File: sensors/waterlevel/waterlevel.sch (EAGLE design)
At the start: 77 parts, among them IC2 MCP604SL, IC3 MCP601SN, IC4 MCP601SN, P1 CAMDEN-CTB5000/6, U1 NCP1729SN35T1G, U2 SR05S05, U3 VISHAY-VCUT05A4, U4 VISHAY-VCUT05A4, U5 LP3981IMM-3.3

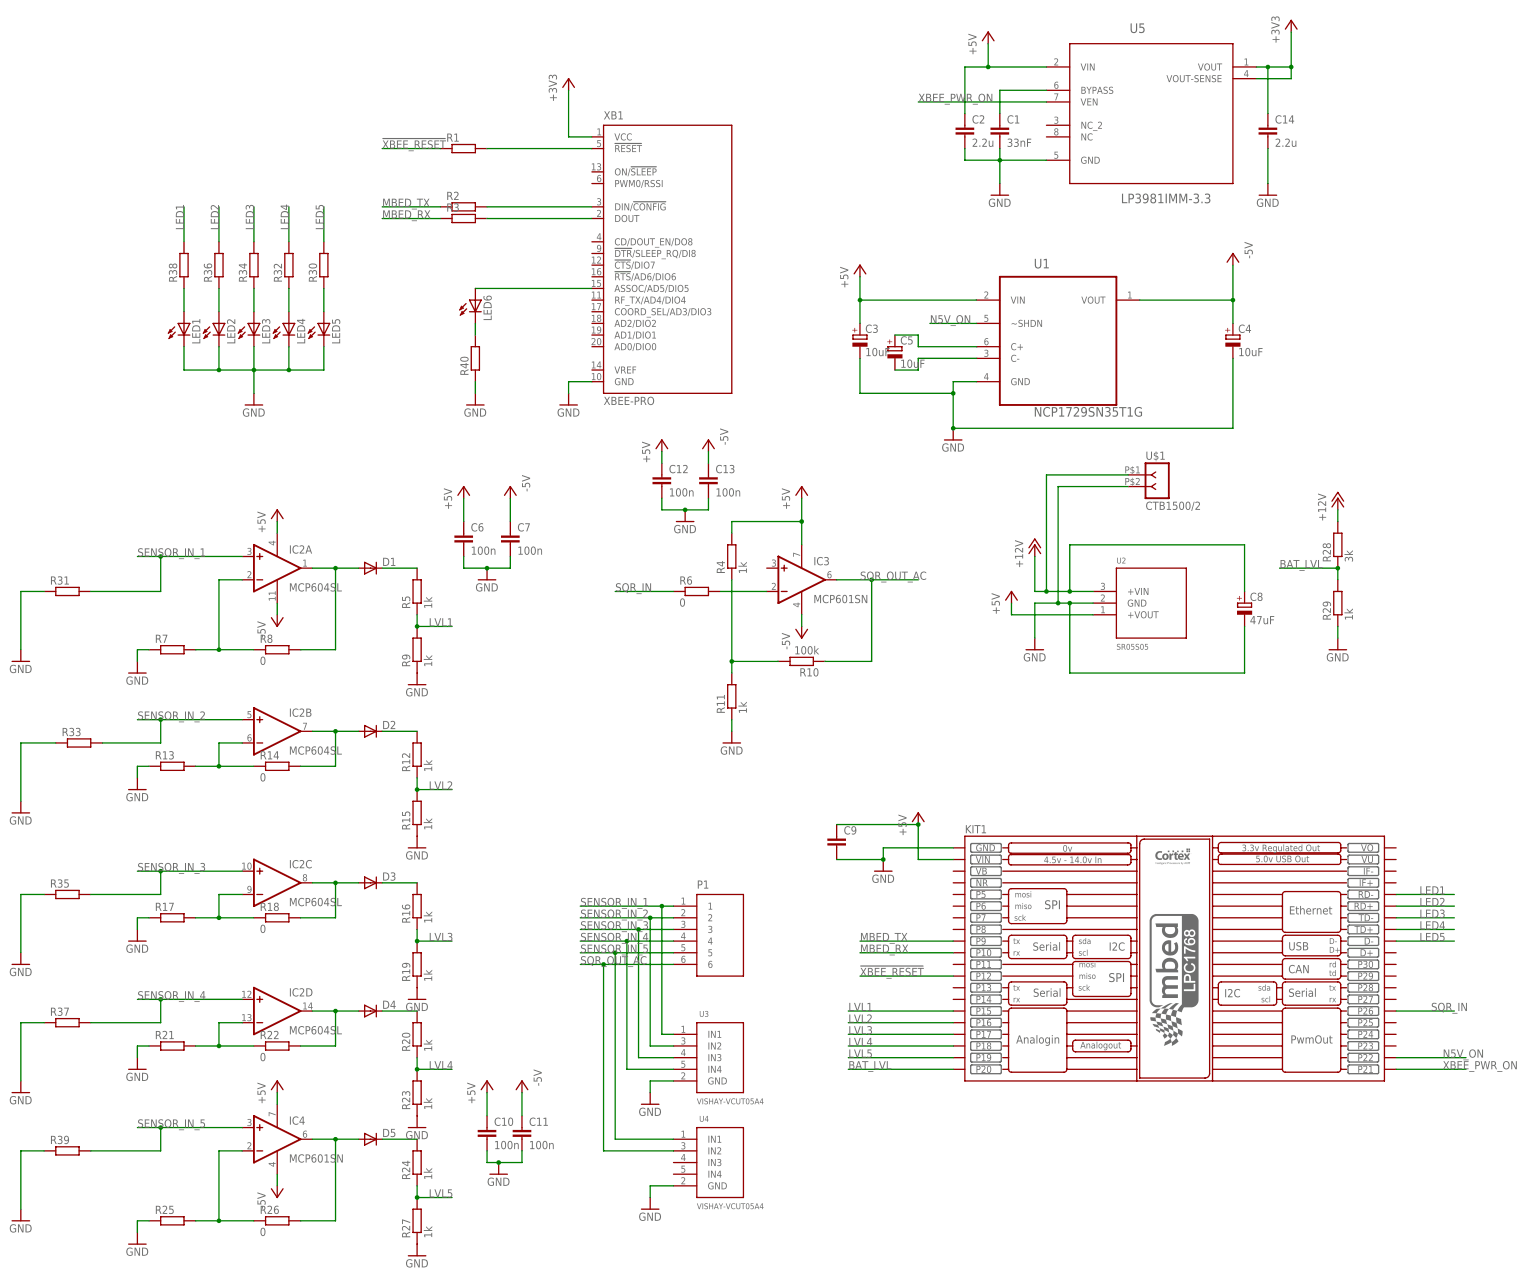
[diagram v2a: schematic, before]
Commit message: Completed water level sensor / wireless network board.
Added status LEDs
Added test points for critical signals
Added M3 mounting holes
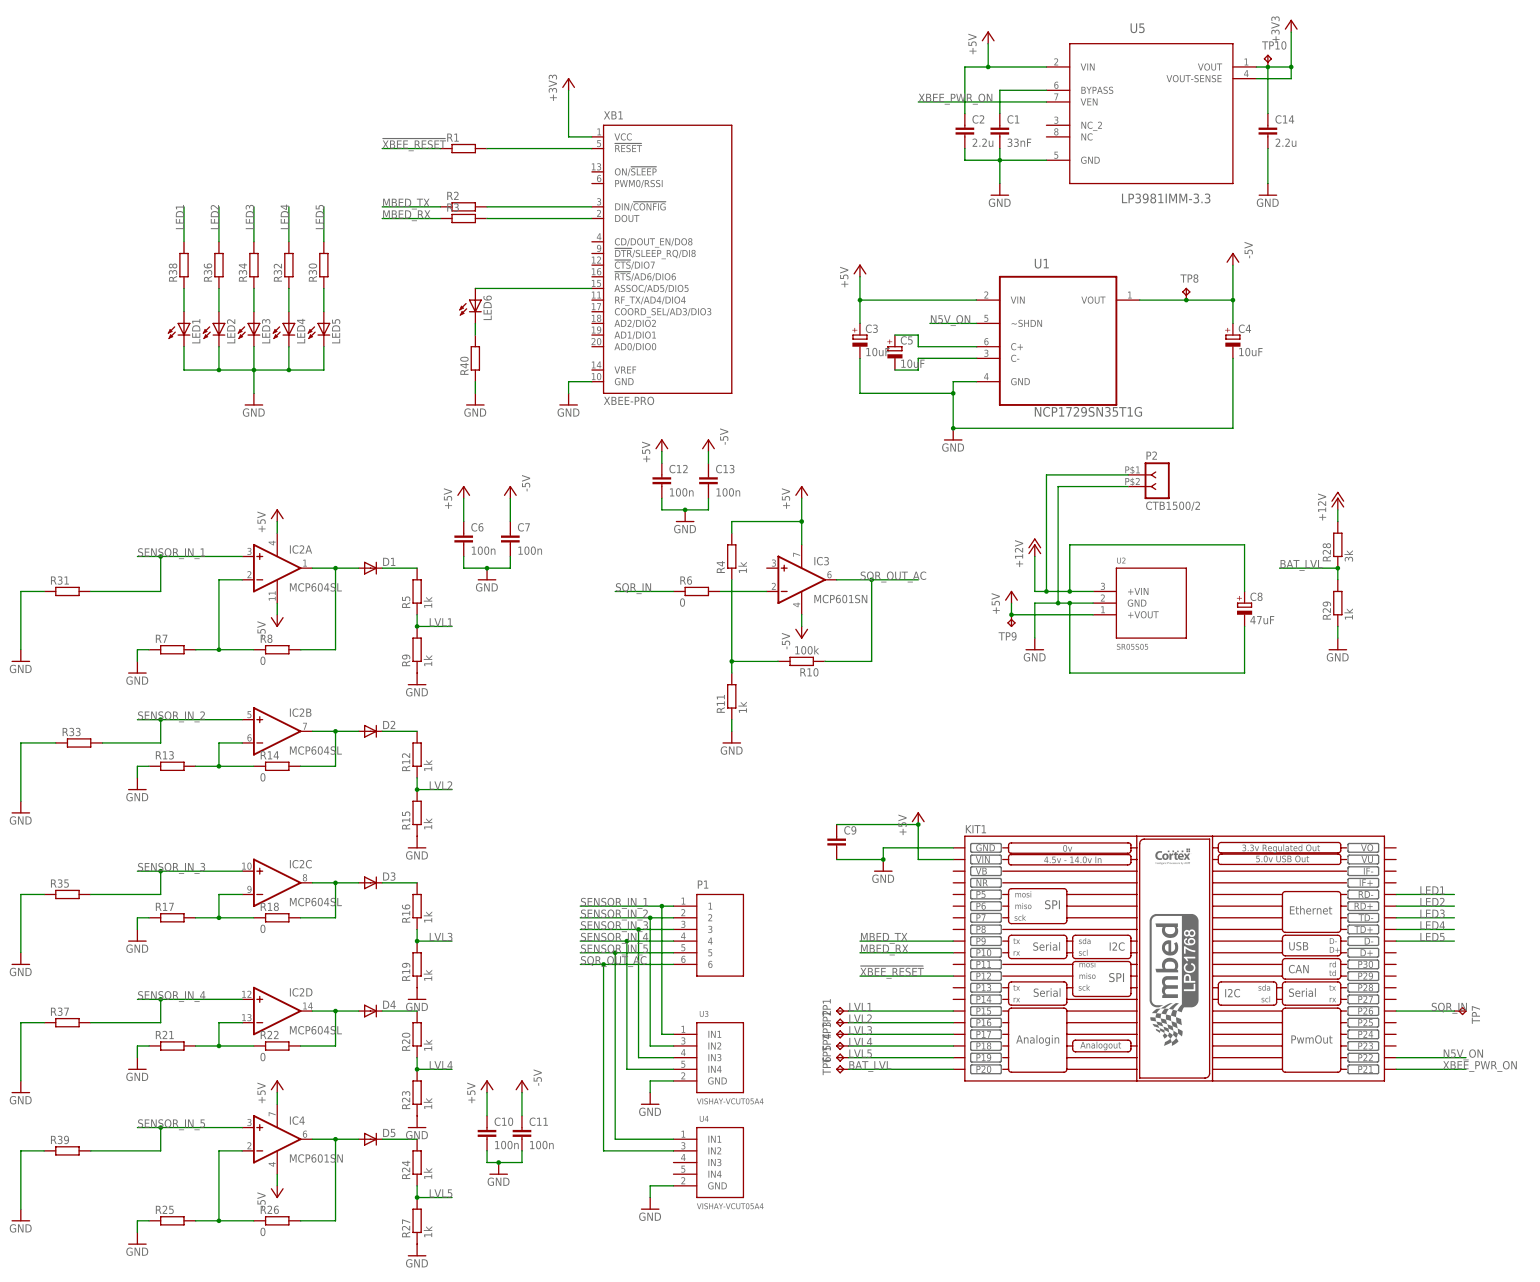
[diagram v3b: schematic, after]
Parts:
- added TP1, TP10, TP2, TP3, TP4, TP5, TP6, TP7, TP8, TP9: TPTP13R, testpad:TPTP13R
- renumbered U$1 to P2
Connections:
- net +3V3: now also TP10.TP
- net +5V: now also TP9.TP
- net -5V: now also TP8.TP
- net BAT_LVL: now also TP6.TP
- net LVL1: now also TP1.TP
- net LVL2: now also TP2.TP
- net LVL3: now also TP3.TP
- net LVL4: now also TP4.TP
- net LVL5: now also TP5.TP
- net SQR_IN: now also TP7.TP
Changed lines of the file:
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@@
 <part name="R2" library="resistor" deviceset="R-EU_" device="R0603"/>
 <part name="R3" library="resistor" deviceset="R-EU_" device="R0603"/>
-<part name="U$1" library="eko-parts" deviceset="CTB1500/2" device=""/>
+<part name="P2" library="eko-parts" deviceset="CTB1500/2" device=""/>
 <part name="C12" library="resistor" deviceset="C-EU" device="C1206" value="100n"/>
 <part name="C13" library="resistor" deviceset="C-EU" device="C1206" value="100n"/>
@@
 <part name="GND29" library="supply1" deviceset="GND" device=""/>
 <part name="GND30" library="supply1" deviceset="GND" device=""/>
+<part name="TP1" library="testpad" deviceset="TP" device="TP13R"/>
+<part name="TP2" library="testpad" deviceset="TP" device="TP13R"/>
+<part name="TP3" library="testpad" deviceset="TP" device="TP13R"/>
+<part name="TP4" library="testpad" deviceset="TP" device="TP13R"/>
+<part name="TP5" library="testpad" deviceset="TP" device="TP13R"/>
+<part name="TP6" library="testpad" deviceset="TP" device="TP13R"/>
+<part name="TP7" library="testpad" deviceset="TP" device="TP13R"/>
+<part name="TP9" library="testpad" deviceset="TP" device="TP13R"/>
+<part name="TP8" library="testpad" deviceset="TP" device="TP13R"/>
+<part name="TP10" library="testpad" deviceset="TP" device="TP13R"/>
 </parts>
 <sheets>
@@
 <instance part="R2" gate="G$1" x="50.8" y="228.6"/>
 <instance part="R3" gate="G$1" x="50.8" y="226.06"/>
-<instance part="U$1" gate="G$1" x="200.66" y="167.64"/>
+<instance part="P2" gate="G$1" x="200.66" y="167.64"/>
 <instance part="C12" gate="G$1" x="93.98" y="170.18"/>
 <instance part="C13" gate="G$1" x="104.14" y="170.18"/>
@@
 <instance part="GND29" gate="1" x="53.34" y="185.42"/>
 <instance part="GND30" gate="1" x="5.08" y="185.42"/>
+<instance part="TP1" gate="G$1" x="132.08" y="53.34" rot="R90"/>
+<instance part="TP2" gate="G$1" x="132.08" y="50.8" rot="R90"/>
+<instance part="TP3" gate="G$1" x="132.08" y="48.26" rot="R90"/>
+<instance part="TP4" gate="G$1" x="132.08" y="45.72" rot="R90"/>
+<instance part="TP5" gate="G$1" x="132.08" y="43.18" rot="R90"/>
+<instance part="TP6" gate="G$1" x="132.08" y="40.64" rot="R90"/>
+<instance part="TP7" gate="G$1" x="269.24" y="53.34" rot="R270"/>
+<instance part="TP9" gate="G$1" x="170.18" y="137.16" rot="R180"/>
+<instance part="TP8" gate="G$1" x="208.28" y="210.82"/>
+<instance part="TP10" gate="G$1" x="226.06" y="261.62"/>
 </instances>
 <busses>
@@
 <segment>
 <pinref part="U1" gate="A" pin="VOUT"/>
-<wire x1="198.12" y1="208.28" x2="218.44" y2="208.28" width="0.1524" layer="91"/>
+<wire x1="198.12" y1="208.28" x2="208.28" y2="208.28" width="0.1524" layer="91"/>
+<wire x1="208.28" y1="208.28" x2="218.44" y2="208.28" width="0.1524" layer="91"/>
 <wire x1="218.44" y1="208.28" x2="218.44" y2="215.9" width="0.1524" layer="91"/>
 <pinref part="P-6" gate="1" pin="-5V"/>
@@
 <wire x1="218.44" y1="208.28" x2="218.44" y2="203.2" width="0.1524" layer="91"/>
 <junction x="218.44" y="208.28"/>
+<pinref part="TP8" gate="G$1" pin="TP"/>
+<junction x="208.28" y="208.28"/>
 </segment>
 <segment>
@@
 <wire x1="187.96" y1="139.7" x2="170.18" y2="139.7" width="0.1524" layer="91"/>
 <wire x1="170.18" y1="139.7" x2="170.18" y2="142.24" width="0.1524" layer="91"/>
+<pinref part="TP9" gate="G$1" pin="TP"/>
+<junction x="170.18" y="139.7"/>
 </segment>
 <segment>
@@
 <wire x1="182.88" y1="127" x2="182.88" y2="142.24" width="0.1524" layer="91"/>
 <junction x="182.88" y="142.24"/>
-<pinref part="U$1" gate="G$1" pin="2"/>
+<pinref part="P2" gate="G$1" pin="2"/>
 <wire x1="195.58" y1="167.64" x2="180.34" y2="167.64" width="0.1524" layer="91"/>
 <wire x1="180.34" y1="167.64" x2="180.34" y2="142.24" width="0.1524" layer="91"/>
@@
 <wire x1="157.48" y1="50.8" x2="134.62" y2="50.8" width="0.1524" layer="91"/>
 <label x="134.62" y="50.8" size="1.778" layer="95"/>
+<pinref part="TP2" gate="G$1" pin="TP"/>
 </segment>
 </net>
@@
 <wire x1="157.48" y1="53.34" x2="134.62" y2="53.34" width="0.1524" layer="91"/>
 <label x="134.62" y="53.34" size="1.778" layer="95"/>
+<pinref part="TP1" gate="G$1" pin="TP"/>
 </segment>
 </net>
@@
 <wire x1="157.48" y1="48.26" x2="134.62" y2="48.26" width="0.1524" layer="91"/>
 <label x="134.62" y="48.26" size="1.778" layer="95"/>
+<pinref part="TP3" gate="G$1" pin="TP"/>
 </segment>
 </net>
@@
 <wire x1="157.48" y1="45.72" x2="134.62" y2="45.72" width="0.1524" layer="91"/>
 <label x="134.62" y="45.72" size="1.778" layer="95"/>
+<pinref part="TP4" gate="G$1" pin="TP"/>
 </segment>
 </net>
@@
 <wire x1="157.48" y1="43.18" x2="134.62" y2="43.18" width="0.1524" layer="91"/>
 <label x="134.62" y="43.18" size="1.778" layer="95"/>
+<pinref part="TP5" gate="G$1" pin="TP"/>
 </segment>
 </net>
@@
 <wire x1="254" y1="53.34" x2="266.7" y2="53.34" width="0.1524" layer="91"/>
 <label x="261.62" y="53.34" size="1.778" layer="95"/>
+<pinref part="TP7" gate="G$1" pin="TP"/>
 </segment>
 </net>
@@
 <wire x1="182.88" y1="154.94" x2="220.98" y2="154.94" width="0.1524" layer="91"/>
 <wire x1="220.98" y1="154.94" x2="220.98" y2="144.78" width="0.1524" layer="91"/>
-<pinref part="U$1" gate="G$1" pin="1"/>
+<pinref part="P2" gate="G$1" pin="1"/>
 <wire x1="195.58" y1="170.18" x2="177.8" y2="170.18" width="0.1524" layer="91"/>
 <wire x1="177.8" y1="170.18" x2="177.8" y2="144.78" width="0.1524" layer="91"/>
@@
 <wire x1="226.06" y1="248.92" x2="226.06" y2="259.08" width="0.1524" layer="91"/>
 <junction x="226.06" y="259.08"/>
+<pinref part="TP10" gate="G$1" pin="TP"/>
 </segment>
 </net>
@@
 <wire x1="157.48" y1="40.64" x2="134.62" y2="40.64" width="0.1524" layer="91"/>
 <label x="134.62" y="40.64" size="1.778" layer="95"/>
-</segment>
-</net>
+<pinref part="TP6" gate="G$1" pin="TP"/>
+</segment>
+</net>
